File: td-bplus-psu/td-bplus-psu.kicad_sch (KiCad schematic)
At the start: 23 parts, among them J1 Conn_01x08_Pin, Q13 BSZ42DN25NS3GATMA1, U14 LT3758AEMSE

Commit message: bplus
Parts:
- Q13: value BSZ42DN25NS3GATMA1 -> (none); Digikey BSZ42DN25NS3GATMA1CT-ND -> (none)
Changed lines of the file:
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@@
       (effects (font (size 1.27 1.27)) (justify left))
     )
-    (property "Value" "BSZ42DN25NS3GATMA1" (at 106.7816 37.973 0)
+    (property "Value" "" (at 106.7816 37.973 0)
       (effects (font (size 1.27 1.27)) (justify left))
     )
@@
       (effects (font (size 1.27 1.27)) (justify left) hide)
     )
-    (property "Digikey" "BSZ42DN25NS3GATMA1CT-ND" (at 101.6 36.83 0)
+    (property "Digikey" "" (at 101.6 36.83 0)
       (effects (font (size 1.27 1.27)) hide)
     )
@@
   (symbol (lib_id "power:HT") (at 60.325 95.25 270) (unit 1)
     (in_bom yes) (on_board yes) (dnp no)
-    (property "Reference" "#PWR0172" (at 63.373 95.25 0)
+    (property "Reference" "#PWR03" (at 63.373 95.25 0)
       (effects (font (size 1.27 1.27)) hide)
     )
@@
   (symbol (lib_id "power:GND") (at 74.93 85.09 0) (unit 1)
     (in_bom yes) (on_board yes) (dnp no)
-    (property "Reference" "#PWR0171" (at 74.93 91.44 0)
+    (property "Reference" "#PWR02" (at 74.93 91.44 0)
       (effects (font (size 1.27 1.27)) hide)
     )
@@
   (symbol (lib_id "power:+48V") (at 69.215 77.47 0) (unit 1)
     (in_bom yes) (on_board yes) (dnp no)
-    (property "Reference" "#PWR0170" (at 69.215 81.28 0)
-      (effects (font (size 1.27 1.27)) hide)
-    )
+    (property "Reference" "#PWR01" (at 69.215 81.28 0)
+      (effects (font (size 1.27 1.27)) hide)
+    )

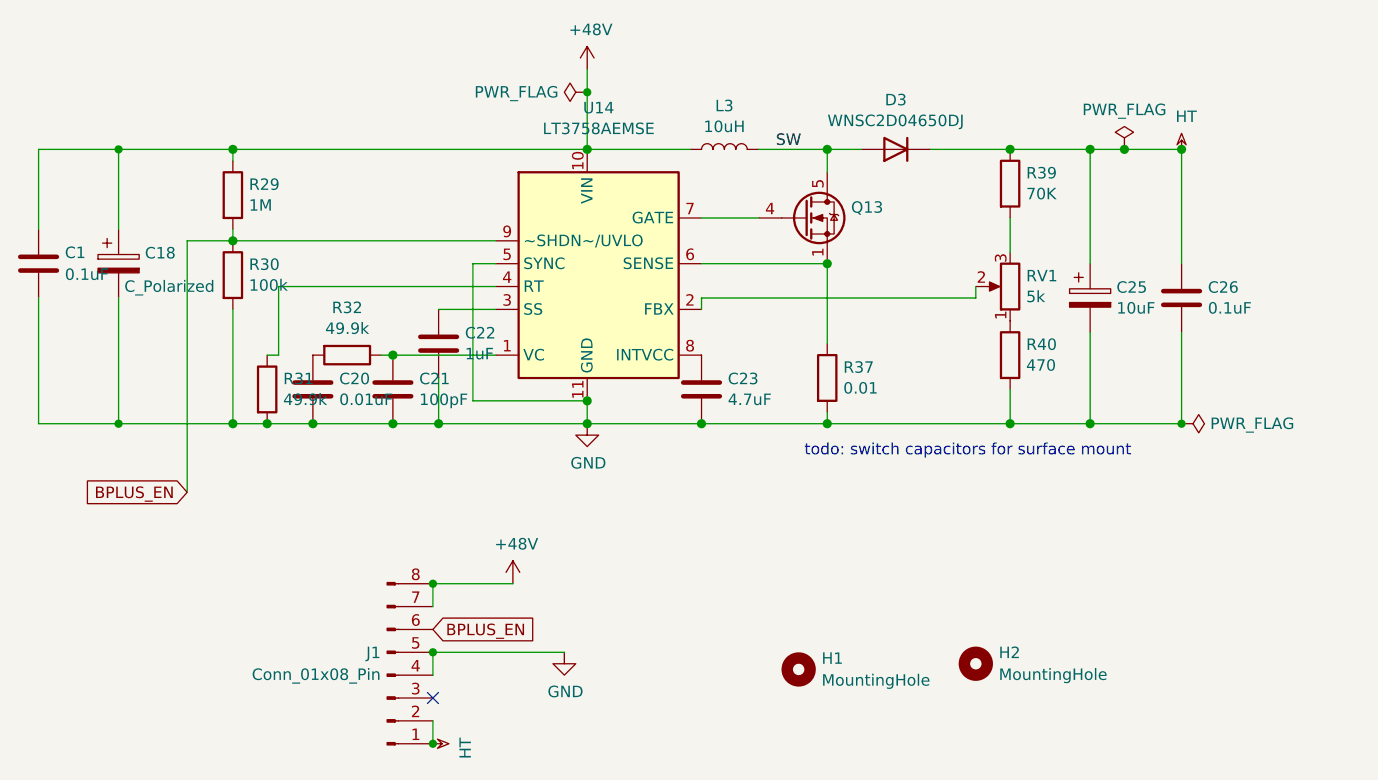
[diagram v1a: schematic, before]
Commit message: Update bplus psu to have better caps and pot facing the right dir
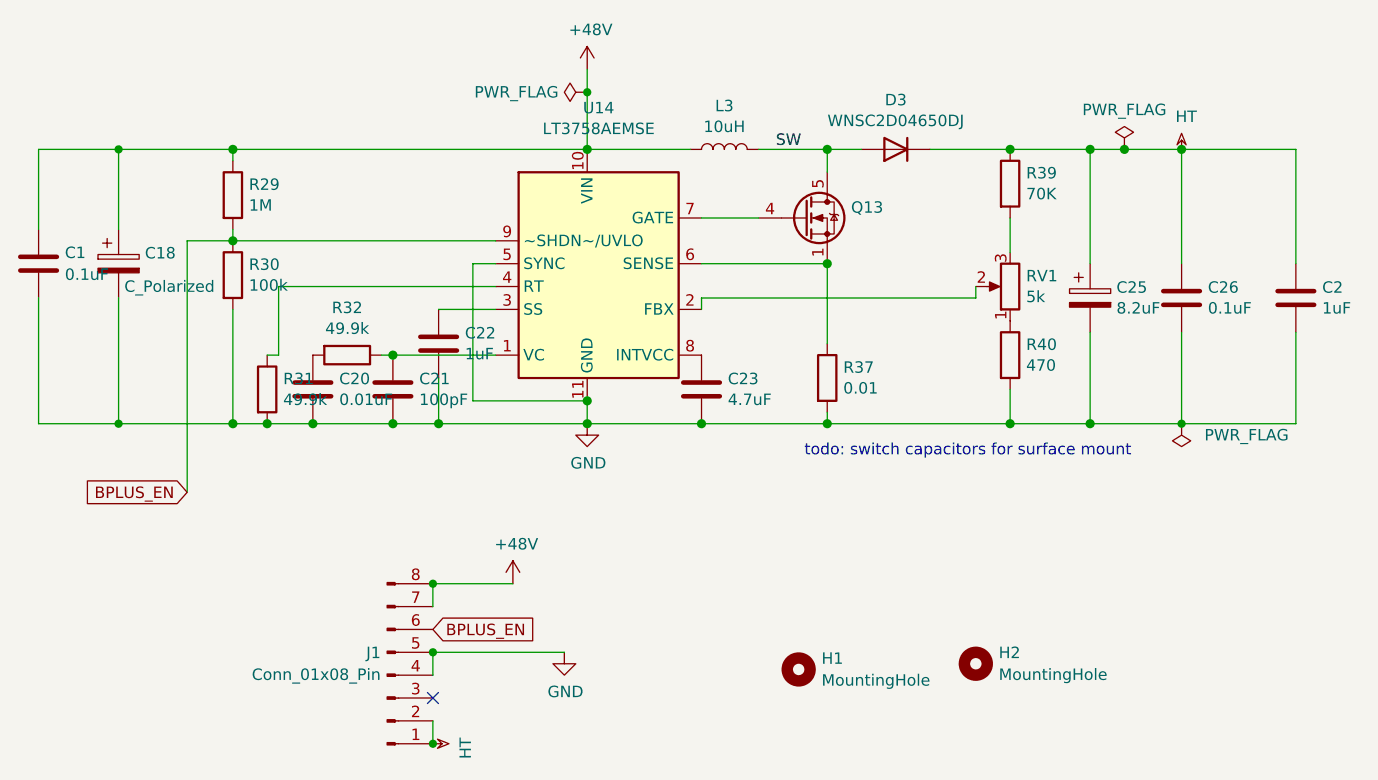
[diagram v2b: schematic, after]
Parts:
- added C2: 1uF, Capacitor_SMD:C_2220_5750Metric_Pad1.97x5.40mm_HandSolder, symbol Device:C
- C25: value 10uF -> 8.2uF; footprint Capacitor_THT:CP_Radial_D8.0mm_P3.50mm -> Capacitor_THT:CP_Radial_D10.0mm_P5.00mm; Digikey 565-5070-ND -> 399-14135-ND
- Q13: value (none) -> ~
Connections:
- net GND: now also C2.2
- net HT: now also C2.1

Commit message: Update bplus psu for better caps
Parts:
- H1, H2: now left out of the parts list
- J1: Digikey (none) -> 10129379-908001BLF-ND
- Q13: Digikey (none) -> BSC600N25NS3GATMA1CT-ND
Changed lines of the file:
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@@
 			)
 		)
-		(property "Digikey" ""
+		(property "Digikey" "BSC600N25NS3GATMA1CT-ND"
 			(at 101.6 36.83 0)
 			(effects
@@
 		(unit 1)
 		(exclude_from_sim no)
-		(in_bom yes)
+		(in_bom no)
 		(on_board yes)
 		(dnp no)
@@
 		(unit 1)
 		(exclude_from_sim no)
-		(in_bom yes)
+		(in_bom no)
 		(on_board yes)
 		(dnp no)
@@
 			)
 		)
+		(property "Digikey" "10129379-908001BLF-ND"
+			(at 55.245 87.63 0)
+			(effects
+				(font
+					(size 1.27 1.27)
+				)
+				(hide yes)
+			)
+		)
